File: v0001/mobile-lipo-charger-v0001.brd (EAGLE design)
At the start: 83 x 93.5 mm, 38 parts, among them IC1 AD8610MR, IC2 STM32F401VBT, IC3 AD8610MR, SW1 DHT-4235A

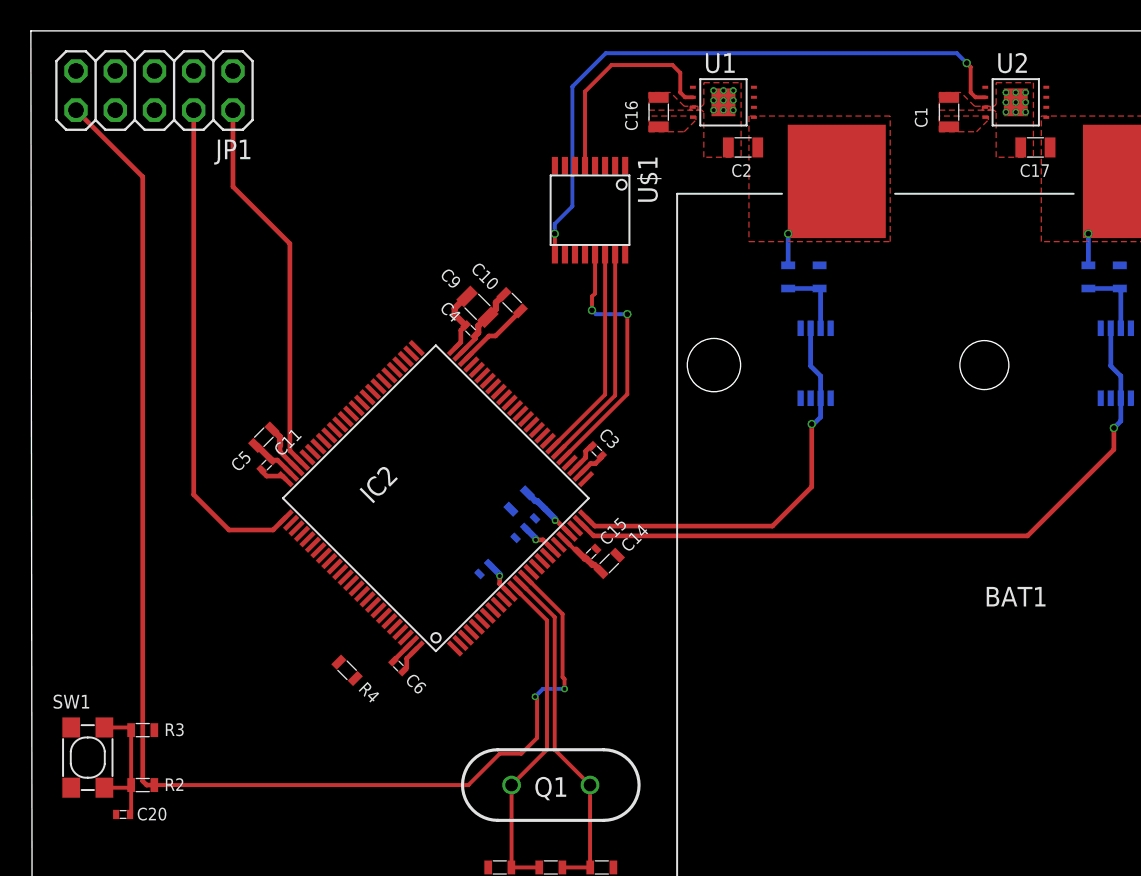
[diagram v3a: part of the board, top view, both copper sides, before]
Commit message: Charger Chip Enable
Routed the charger chip enable lines.
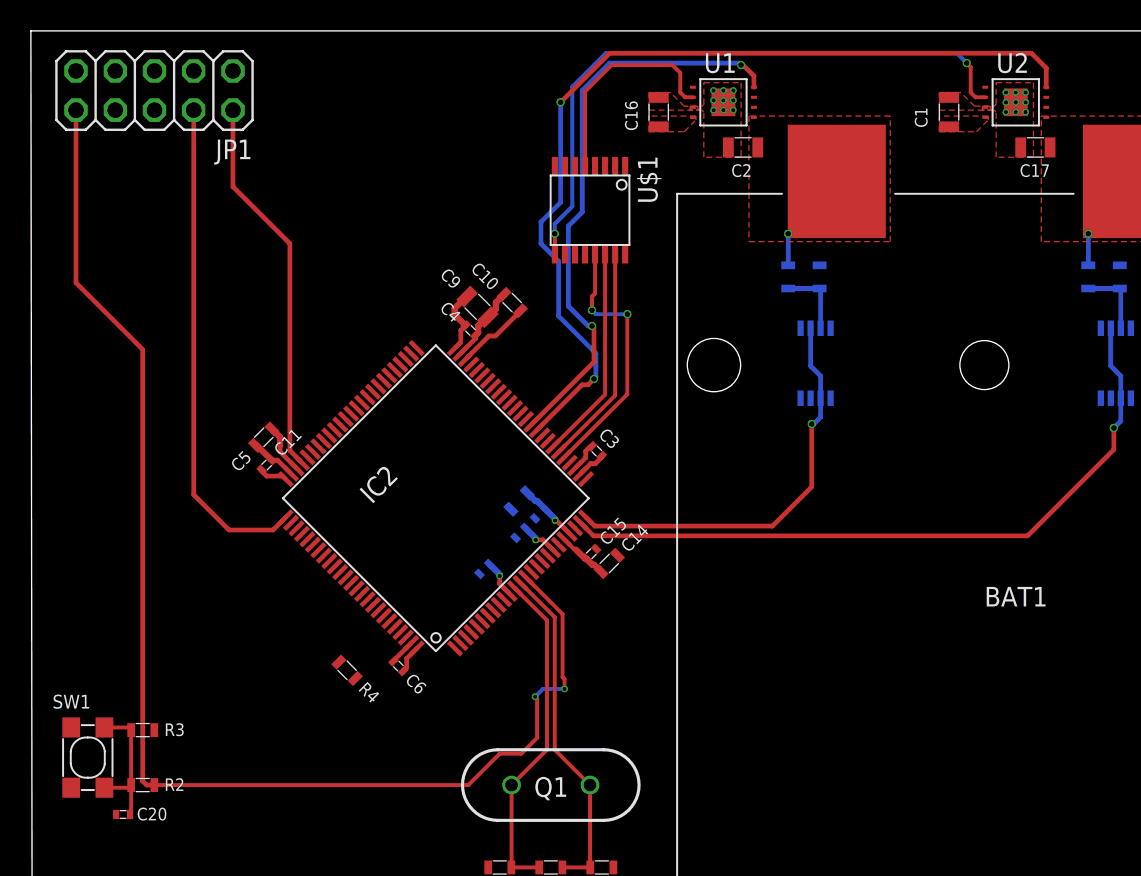
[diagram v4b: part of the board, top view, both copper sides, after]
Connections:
- net BATT1_CE: now also IC2.36
- net BATT2_CE: now also IC2.35
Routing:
- net BATT2_CE: track 0.00 -> 59.4 mm, vias 0 -> 2
- net BATT1_CE: track 0.00 -> 37.4 mm, vias 0 -> 2
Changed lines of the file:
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@@
 <signal name="BATT1_CE">
 <contactref element="U1" pad="8"/>
+<contactref element="IC2" pad="36"/>
+<wire x1="46.679" y1="100.797" x2="46.679" y2="101.53" width="0.3048" layer="1"/>
+<wire x1="45.974" y1="102.235" x2="45.847" y2="102.235" width="0.3048" layer="1"/>
+<via x="45.847" y="102.235" extent="1-16" drill="0.35"/>
+<wire x1="45.847" y1="102.235" x2="45.72" y2="102.362" width="0.3048" layer="16"/>
+<wire x1="37.338" y1="102.362" x2="35.56" y2="100.584" width="0.3048" layer="16"/>
+<wire x1="35.56" y1="92.71" x2="34.671" y2="91.821" width="0.3048" layer="16"/>
+<wire x1="34.671" y1="91.821" x2="34.671" y2="86.614" width="0.3048" layer="16"/>
+<wire x1="35.941" y1="85.344" x2="36.195" y2="85.344" width="0.3048" layer="16"/>
+<via x="36.195" y="85.344" extent="1-16" drill="0.35"/>
+<wire x1="36.322" y1="85.217" x2="36.195" y2="85.344" width="0.3048" layer="1"/>
+<wire x1="46.679" y1="101.53" x2="45.974" y2="102.235" width="0.3048" layer="1"/>
+<wire x1="45.72" y1="102.362" x2="37.338" y2="102.362" width="0.3048" layer="16"/>
+<wire x1="35.56" y1="100.584" x2="35.56" y2="92.71" width="0.3048" layer="16"/>
+<wire x1="34.671" y1="86.614" x2="35.941" y2="85.344" width="0.3048" layer="16"/>
+<wire x1="32.274784375" y1="78.962753125" x2="36.322" y2="83.00996875" width="0.3048" layer="1"/>
+<wire x1="36.322" y1="83.00996875" x2="36.322" y2="85.217" width="0.3048" layer="1"/>
 </signal>
 <signal name="BATT1_ISET">
@@
 <signal name="BATT2_CE">
 <contactref element="U2" pad="8"/>
+<contactref element="IC2" pad="35"/>
+<wire x1="65.602" y1="100.797" x2="65.602" y2="102.038" width="0.3048" layer="1"/>
+<wire x1="65.602" y1="102.038" x2="64.643" y2="102.997" width="0.3048" layer="1"/>
+<wire x1="64.643" y1="102.997" x2="37.338" y2="102.997" width="0.3048" layer="1"/>
+<via x="34.163" y="99.822" extent="1-16" drill="0.35"/>
+<wire x1="34.163" y1="99.822" x2="34.163" y2="93.345" width="0.3048" layer="16"/>
+<wire x1="32.893" y1="90.678" x2="34.036" y2="89.535" width="0.3048" layer="16"/>
+<wire x1="34.036" y1="85.979" x2="36.449" y2="83.566" width="0.3048" layer="16"/>
+<wire x1="36.449" y1="83.566" x2="36.449" y2="82.042" width="0.3048" layer="16"/>
+<wire x1="36.449" y1="82.042" x2="36.322" y2="81.915" width="0.3048" layer="16"/>
+<via x="36.322" y="81.915" extent="1-16" drill="0.35"/>
+<wire x1="35.941" y1="81.534" x2="36.322" y2="81.915" width="0.3048" layer="1"/>
+<wire x1="37.338" y1="102.997" x2="34.163" y2="99.822" width="0.3048" layer="1"/>
+<wire x1="34.163" y1="93.345" x2="32.893" y2="92.075" width="0.3048" layer="16"/>
+<wire x1="32.893" y1="92.075" x2="32.893" y2="90.678" width="0.3048" layer="16"/>
+<wire x1="34.036" y1="89.535" x2="34.036" y2="85.979" width="0.3048" layer="16"/>
+<wire x1="32.628340625" y1="78.6092" x2="35.553140625" y2="81.534" width="0.3048" layer="1"/>
+<wire x1="35.553140625" y1="81.534" x2="35.941" y2="81.534" width="0.3048" layer="1"/>
 </signal>
 <signal name="BATT2_OUT">
@@
 <wire x1="34.29" y1="66.694490625" x2="34.29" y2="62.611" width="0.254" layer="1"/>
 <contactref element="JP1" pad="10"/>
-<wire x1="2.794" y1="99.314" x2="7.112" y2="94.996" width="0.3048" layer="1"/>
 <wire x1="7.112" y1="55.88" x2="7.366" y2="55.626" width="0.3048" layer="1"/>
 <wire x1="7.366" y1="55.626" x2="7.862" y2="55.626" width="0.3048" layer="1"/>
-<wire x1="7.112" y1="94.996" x2="7.112" y2="55.88" width="0.3048" layer="1"/>
+<wire x1="7.112" y1="83.82" x2="7.112" y2="55.88" width="0.3048" layer="1"/>
+<wire x1="2.794" y1="99.314" x2="2.794" y2="88.138" width="0.3048" layer="1"/>
+<wire x1="2.794" y1="88.138" x2="7.112" y2="83.82" width="0.3048" layer="1"/>
 </signal>
 <signal name="RST_BUTTON">

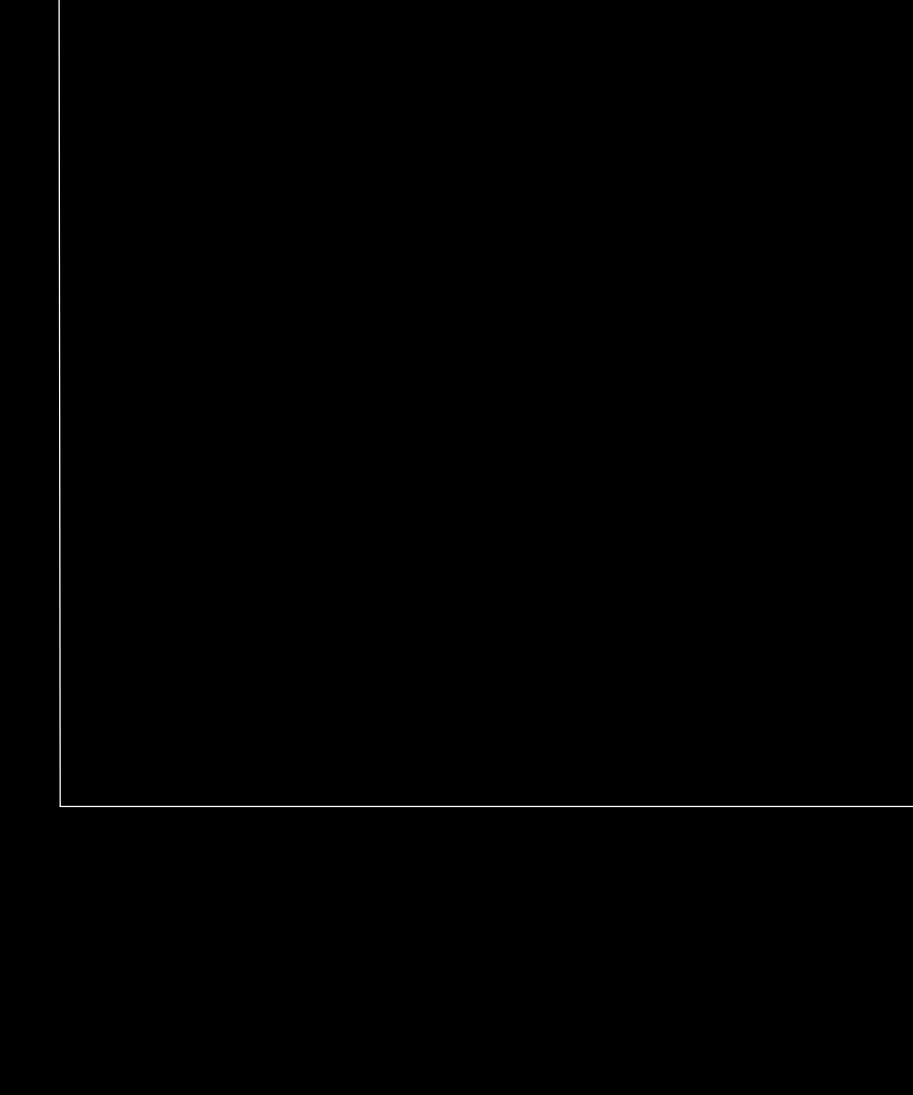
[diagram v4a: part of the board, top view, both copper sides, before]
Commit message: Added 3.3V rail
Added the 3.3V rail switching supply
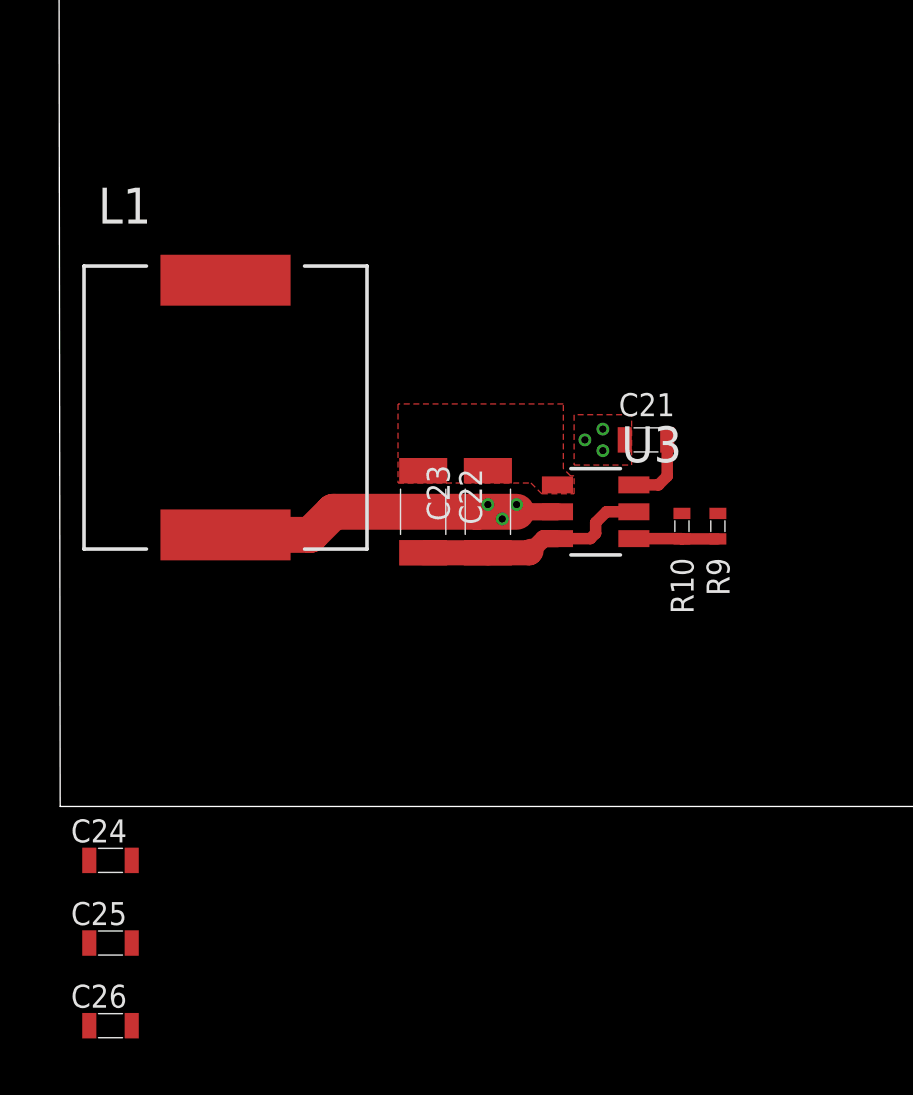
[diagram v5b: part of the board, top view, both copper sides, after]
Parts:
- added C21: 100n, common:0603L3
- added C22, C23: 10u, common:1206L3
- added C24, C25, C26: 22u, common:0603L3
- added L1: 2.2uH, common:10X10
- added R10: 10k, common:0402L3
- added R9: 33.2k, common:0402L3
- added U3: 3.3V, common:SOT-1.1
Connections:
- new net SW: C21.P$1, L1.1, U3.2
- new net VBST: C21.P$2, U3.6
- new net VFB: R10.P$2, R9.P$1, U3.4
- net BATT+: now also C22.1, C23.1, U3.3, U3.5
- net GND: now also C22.2, C23.2, C24.P$2, C25.P$2, C26.P$2, R10.P$1, U3.1
- net VDD: now also C24.P$1, C25.P$1, C26.P$1, L1.2, R9.P$2
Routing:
- net SW: track 0.00 -> 15.8 mm, vias 0 -> 6
- net BATT+: track 0.00 -> 8.27 mm
- net VFB: track 0.00 -> 2.97 mm
- net VBST: track 0.00 -> 2.59 mm
- added copper zone on layer 1, net SW
- added copper zone on layer 2, net SW

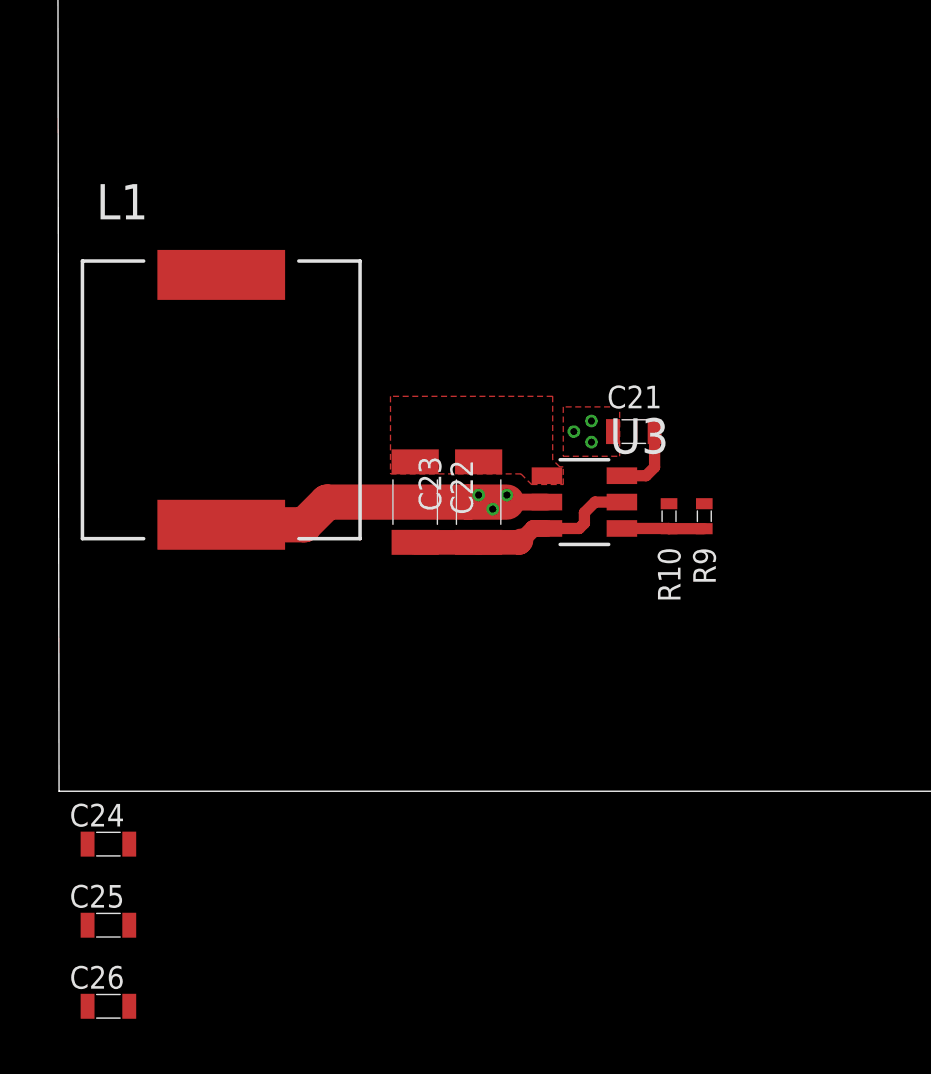
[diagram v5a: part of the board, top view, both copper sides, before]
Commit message: Minor Changes
Made minor changes to the polygons for the charger chips
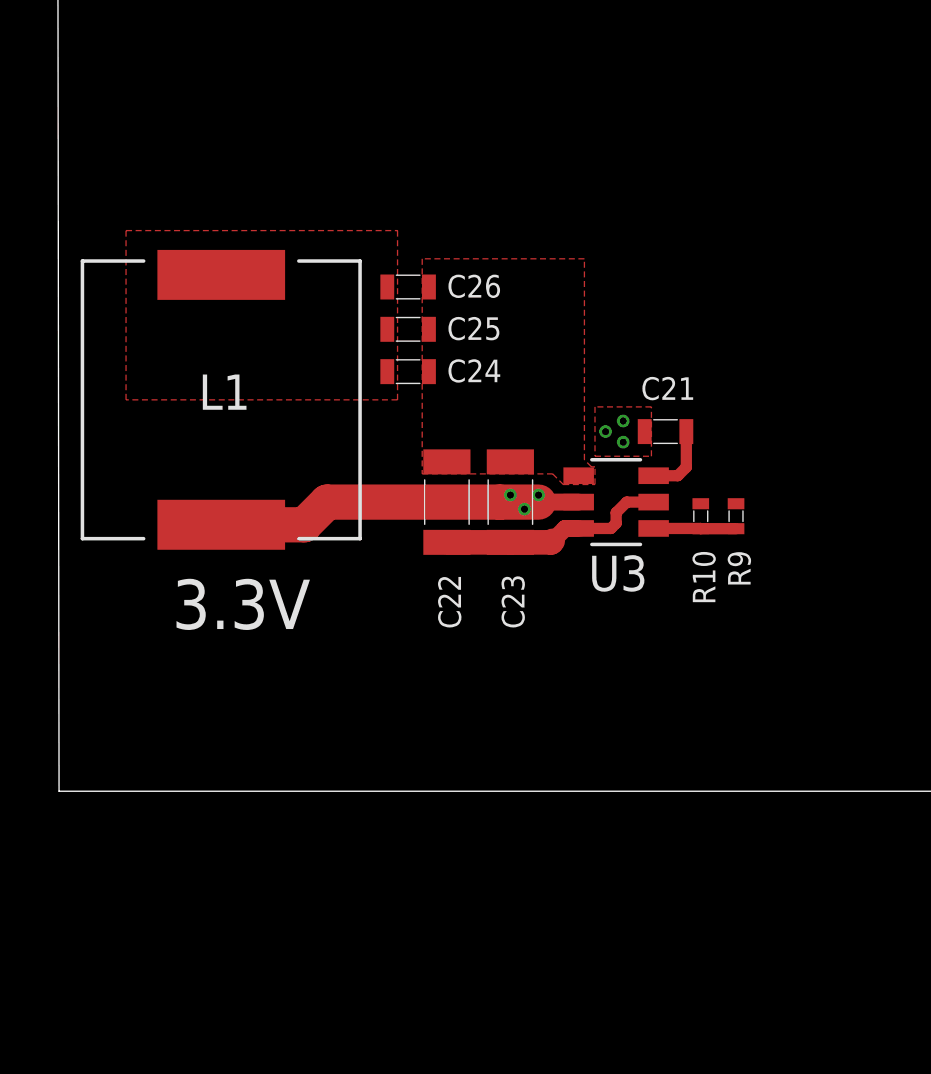
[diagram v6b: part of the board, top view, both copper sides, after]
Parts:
- moved C26 28.1 mm to (12.6, 29.1)
- moved C25 24.0 mm to (12.6, 27.6)
- moved C24 20.2 mm to (12.6, 26.0)
- moved C21 1.14 mm to (21.8, 23.9)
- moved C22 1.14 mm to (14.0, 21.3)
- moved C23 1.14 mm to (16.3, 21.3)
- moved R10 1.14 mm to (23.1, 20.8)
- moved R9 1.14 mm to (24.4, 20.8)
- moved U3 1.14 mm to (20.1, 21.3)
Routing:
- net SW: track 15.8 -> 16.9 mm
- added copper zone on layer 1, net VDD
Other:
- board text added: "3.3V"
